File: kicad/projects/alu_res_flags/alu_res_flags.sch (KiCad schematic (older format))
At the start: 56 parts, among them J1 RES_CRRYBRRW_EQ_IN, J2 Aux_connection, J3 Bus_connection, J4 Control_signal_backplane, J5 ECNZ_OUT, U1 74HCT04, U10 74HCT245, U11 74HCT173, U12 74HCT245, U2 74HCT377, U3 74HCT377, U4 74HCT245, U5 74HCT245, U6 74HCT27, U7 74HCT27, U8 74HCT30, U9 74HCT245

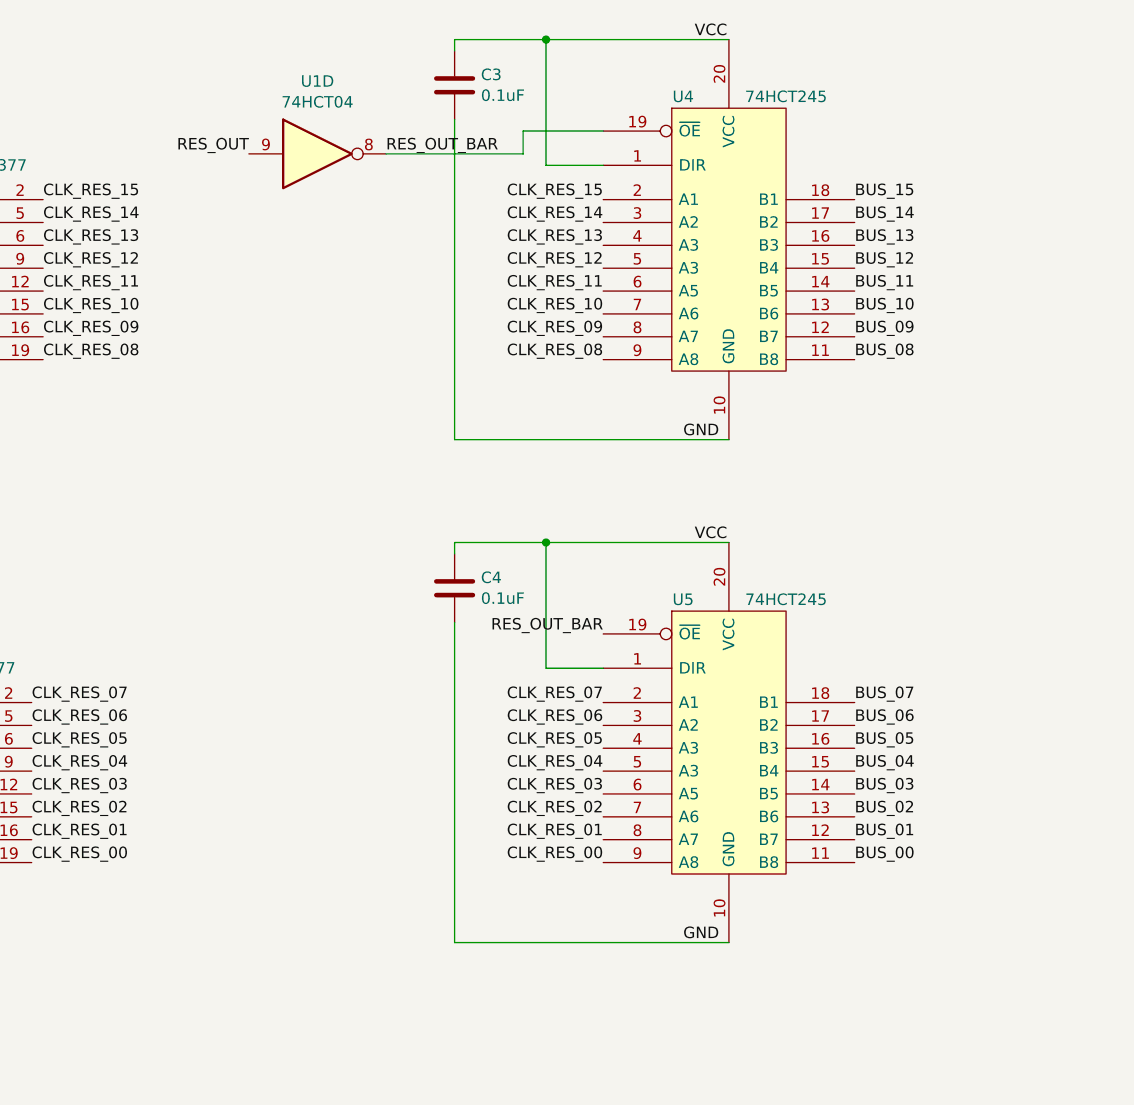
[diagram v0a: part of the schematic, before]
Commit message: Initial component placement
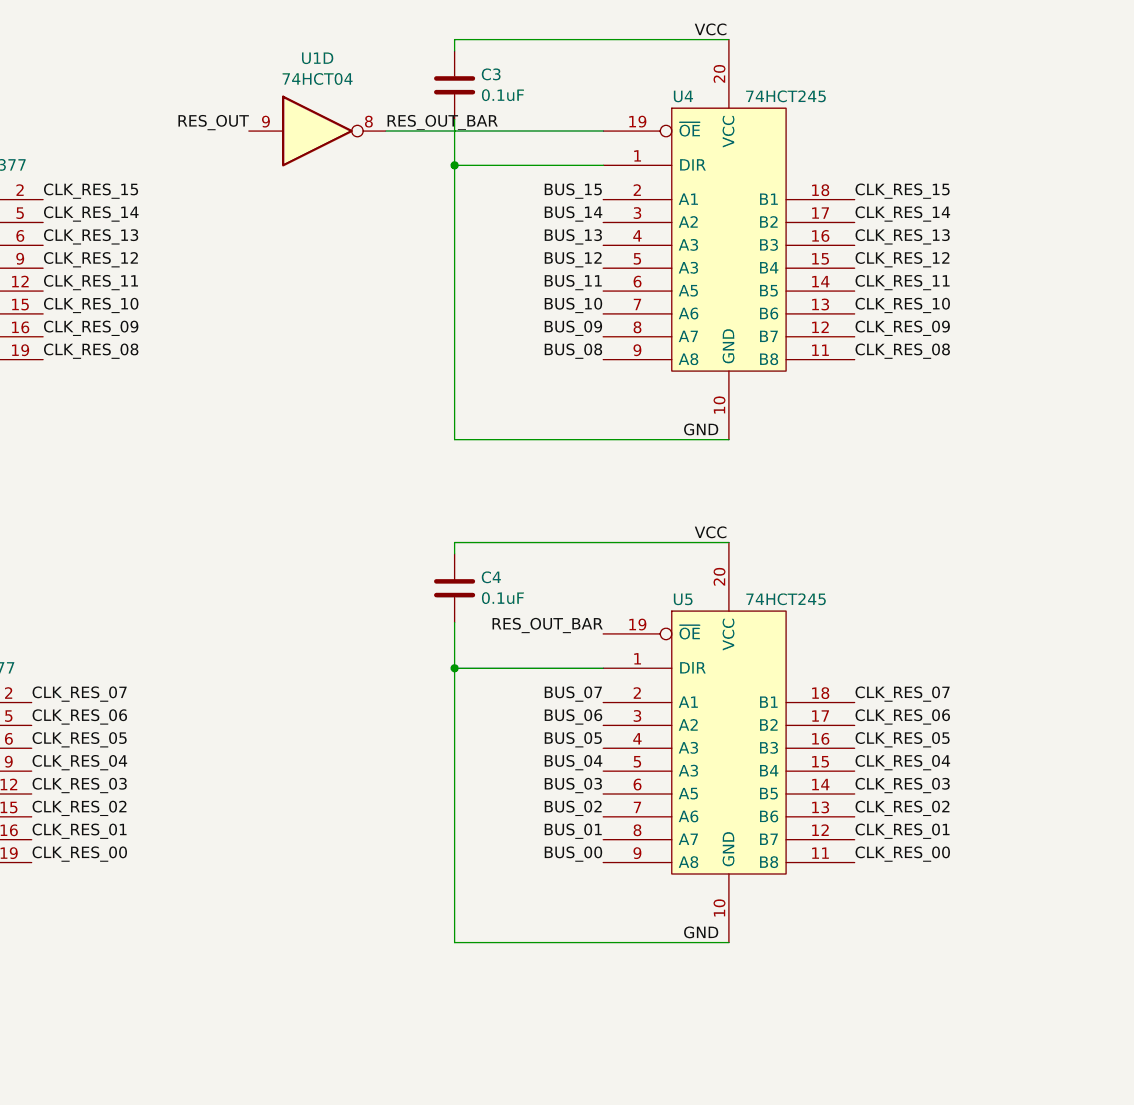
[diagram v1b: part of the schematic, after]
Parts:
- C1, C10, C11, C12, C2, C3, C4, C5, C6, C7, C8, C9: footprint (none) -> Capacitor_THT:C_Disc_D4.7mm_W2.5mm_P5.00mm
- D1, D10, D11, D12, D13, D14, D15, D16, D17, D18, D19, D2, D20, D21, D22, D23, D24, D3, D4, D5, D6, D7, D8, D9: footprint (none) -> eight-bit-computer:LED_D5.0mm_Horizontal_O3.81mm_Z3.0mm
- J1: footprint (none) -> Connector_PinSocket_2.54mm:PinSocket_1x19_P2.54mm_Horizontal
- J2: footprint (none) -> Connector_PinHeader_2.54mm:PinHeader_1x10_P2.54mm_Horizontal
- J3: footprint (none) -> Connector_PinHeader_2.54mm:PinHeader_1x16_P2.54mm_Horizontal
- J4: footprint (none) -> eight-bit-computer:backplane-connector
- J5: footprint (none) -> Connector_PinSocket_2.54mm:PinSocket_1x04_P2.54mm_Horizontal
- U1, U6, U7, U8: footprint (none) -> Package_DIP:DIP-14_W7.62mm_Socket
- U10, U12, U2, U3, U4, U5, U9: footprint (none) -> Package_DIP:DIP-20_W7.62mm_Socket
- U11: footprint (none) -> Package_DIP:DIP-16_W7.62mm_Socket
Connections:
- net BUS_00: now also U5.9 (A8); no longer U5.11 (B8)
- net BUS_01: now also U5.8 (A7); no longer U5.12 (B7)
- net BUS_02: now also U5.7 (A6); no longer U5.13 (B6)
- net BUS_03: now also U5.6 (A5); no longer U5.14 (B5)
- net BUS_04: now also U5.5 (A3); no longer U5.15 (B4)
- net BUS_05: now also U5.4 (A3); no longer U5.16 (B3)
- net BUS_06: now also U5.3 (A2); no longer U5.17 (B2)
- net BUS_07: now also U5.2 (A1); no longer U5.18 (B1)
- net BUS_08: now also U4.9 (A8); no longer U4.11 (B8)
- net BUS_09: now also U4.8 (A7); no longer U4.12 (B7)
- net BUS_10: now also U4.7 (A6); no longer U4.13 (B6)
- net BUS_11: now also U4.6 (A5); no longer U4.14 (B5)
- net BUS_12: now also U4.5 (A3); no longer U4.15 (B4)
- net BUS_13: now also U4.4 (A3); no longer U4.16 (B3)
- net BUS_14: now also U4.3 (A2); no longer U4.17 (B2)
- net BUS_15: now also U4.2 (A1); no longer U4.18 (B1)
- net CLK_RES_00: now also U5.11 (B8); no longer U5.9 (A8)
- net CLK_RES_01: now also U5.12 (B7); no longer U5.8 (A7)
- net CLK_RES_02: now also U5.13 (B6); no longer U5.7 (A6)
- net CLK_RES_03: now also U5.14 (B5); no longer U5.6 (A5)
- net CLK_RES_04: now also U5.15 (B4); no longer U5.5 (A3)
- net CLK_RES_05: now also U5.16 (B3); no longer U5.4 (A3)
- net CLK_RES_06: now also U5.17 (B2); no longer U5.3 (A2)
- net CLK_RES_07: now also U5.18 (B1); no longer U5.2 (A1)
- net CLK_RES_08: now also U4.11 (B8); no longer U4.9 (A8)
- net CLK_RES_09: now also U4.12 (B7); no longer U4.8 (A7)
- net CLK_RES_10: now also U4.13 (B6); no longer U4.7 (A6)
- net CLK_RES_11: now also U4.14 (B5); no longer U4.6 (A5)
- net CLK_RES_12: now also U4.15 (B4); no longer U4.5 (A3)
- net CLK_RES_13: now also U4.16 (B3); no longer U4.4 (A3)
- net CLK_RES_14: now also U4.17 (B2); no longer U4.3 (A2)
- net CLK_RES_15: now also U4.18 (B1); no longer U4.2 (A1)
- net GND: now also U4.1 (DIR), U5.1 (DIR)
- net VCC: no longer U4.1 (DIR), U5.1 (DIR)
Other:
- moved on the sheet: U1D

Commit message: Starting to route PCB.
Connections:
- net NEGATIVE renamed RES_15
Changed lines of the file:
@@
 Text Label 13300 8300 2    50   ~ 0
 CARRYBORROW
-Text Label 13300 8400 2    50   ~ 0
-NEGATIVE
 Text Label 13300 8500 2    50   ~ 0
 ZERO
@@
 Text Label 15950 7900 2    50   ~ 0
 CARRYBORROW
-Text Label 15950 8000 2    50   ~ 0
-NEGATIVE
 Text Label 15950 8100 2    50   ~ 0
 ZERO
@@
 	9550 4300 9550 4350
 Connection ~ 9550 4350
-Text Label 2700 9850 0    50   ~ 0
-NEGATIVE
-Wire Wire Line
-	2400 9850 2700 9850
 Wire Wire Line
 	5600 3900 6800 3900
@@
 Wire Wire Line
 	5300 2100 6250 2100
+Text Label 13300 8400 2    50   ~ 0
+RES_15
+Text Label 15950 8000 2    50   ~ 0
+RES_15
 $EndSCHEMATC

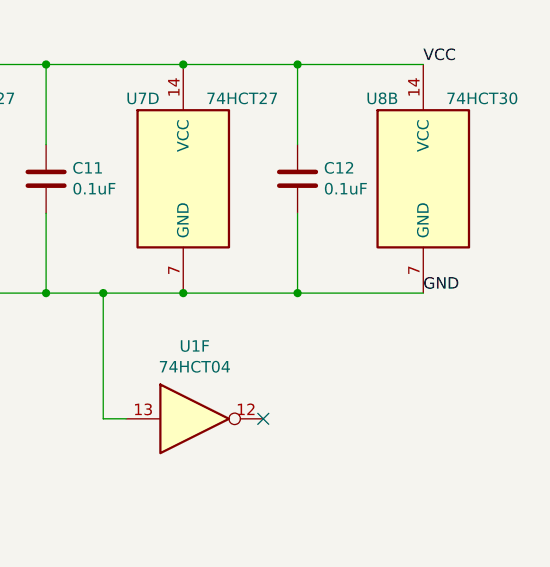
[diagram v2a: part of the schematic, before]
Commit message: Update HCT30 symbol and pins, more PCB routing.
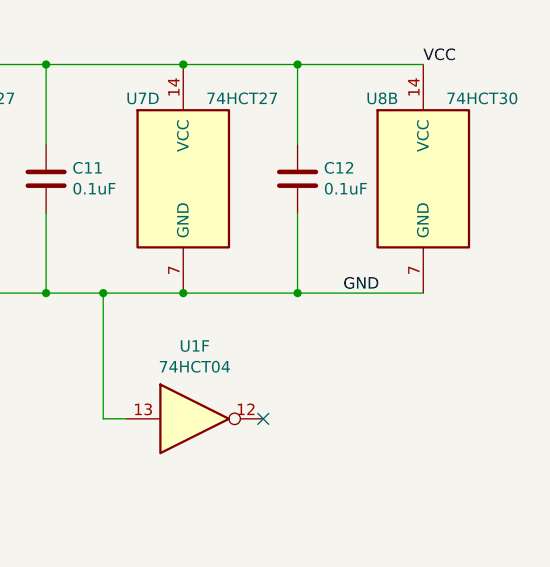
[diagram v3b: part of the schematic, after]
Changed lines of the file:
@@
 Text Label 19750 3250 0    50   ~ 0
 VCC
-Text Label 19750 4250 0    50   ~ 0
+Text Label 19400 4250 0    50   ~ 0
 GND
 NoConn ~ 19050 4800

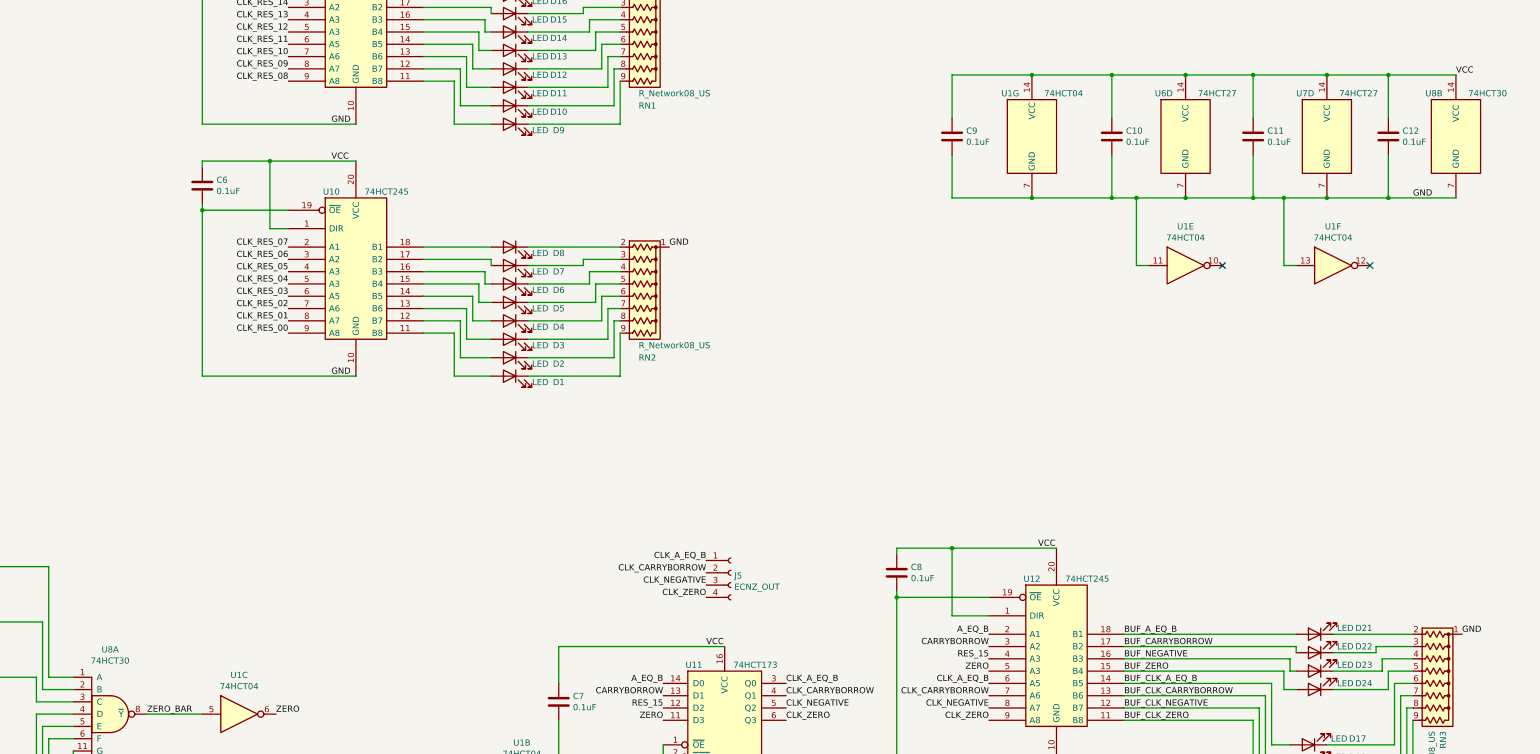
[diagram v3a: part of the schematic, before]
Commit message: Added almost all but LEDs to PCB
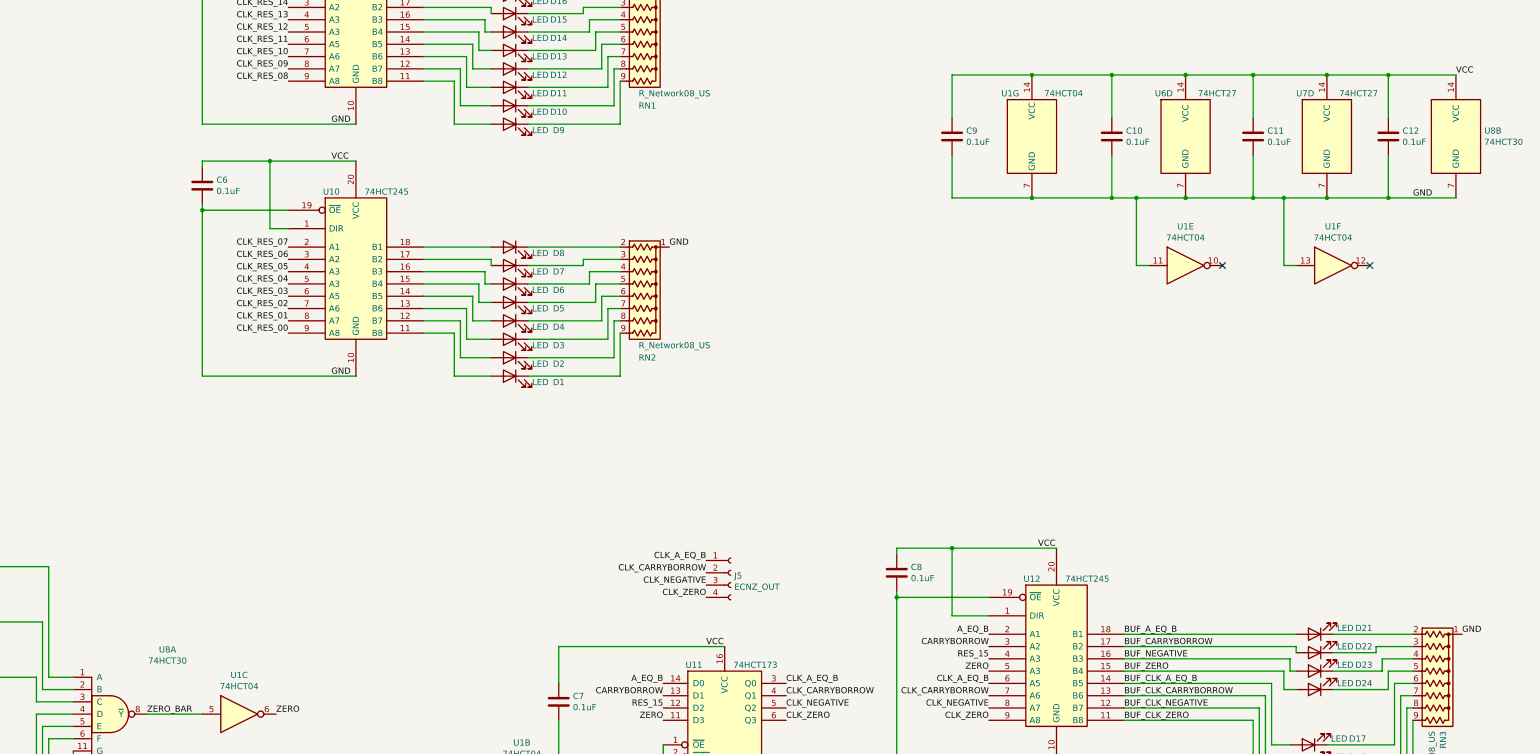
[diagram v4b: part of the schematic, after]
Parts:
- J1: footprint Connector_PinSocket_2.54mm:PinSocket_1x19_P2.54mm_Horizontal -> Connector_PinSocket_2.54mm:PinSocket_1x18_P2.54mm_Horizontal
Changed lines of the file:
@@
-$EndComp
-$Comp
-L eight-bit-computer:74HCT30 U8
-U 1 1 5FB1A22C
-P 8800 8450
-F 0 "U8" H 8800 8975 50  0000 C CNN
-F 1 "74HCT30" H 8800 8884 50  0000 C CNN
-F 2 "Package_DIP:DIP-14_W7.62mm_Socket" H 8800 8450 50  0001 C CNN
-F 3 "https://www.ti.com/lit/ds/symlink/cd74hct30.pdf" H 8800 8450 50  0001 C CNN
-	1    8800 8450
-	1    0    0    -1
-$EndComp
-$Comp
-L eight-bit-computer:74HCT30 U8
-U 2 1 5FB1BA54
-P 19750 3750
-F 0 "U8" H 19500 4100 50  0000 L CNN
-F 1 "74HCT30" H 19850 4100 50  0000 L CNN
-F 2 "Package_DIP:DIP-14_W7.62mm_Socket" H 19750 3750 50  0001 C CNN
-F 3 "https://www.ti.com/lit/ds/symlink/cd74hct30.pdf" H 19750 3750 50  0001 C CNN
-	2    19750 3750
-	1    0    0    -1
 $EndComp
 $Comp
@@
 F 0 "J1" H 2228 9126 50  0000 L CNN
 F 1 "RES_CRRYBRRW_EQ_IN" H 2228 9035 50  0000 L CNN
-F 2 "Connector_PinSocket_2.54mm:PinSocket_1x19_P2.54mm_Horizontal" H 2200 9150 50  0001 C CNN
+F 2 "Connector_PinSocket_2.54mm:PinSocket_1x18_P2.54mm_Horizontal" H 2200 9150 50  0001 C CNN
 F 3 "~" H 2200 9150 50  0001 C CNN
 	1    2200 9150
@@
 Text Label 15950 8000 2    50   ~ 0
 RES_15
+$Comp
+L eight-bit-computer:74HCT30 U8
+U 1 1 5FBBC8A7
+P 8800 8450
+F 0 "U8" H 9267 8975 50  0000 C CNN
+F 1 "74HCT30" H 9267 8884 50  0000 C CNN
+F 2 "Package_DIP:DIP-14_W7.62mm_Socket" H 8800 8450 50  0001 C CNN
+F 3 "https://www.ti.com/lit/ds/symlink/cd74hct30.pdf" H 8800 8450 50  0001 C CNN
+	1    8800 8450
+	1    0    0    -1
+$EndComp
+$Comp
+L eight-bit-computer:74HCT30 U8
+U 2 1 5FBBF1CA
+P 19750 3750
+F 0 "U8" H 19980 3796 50  0000 L CNN
+F 1 "74HCT30" H 19980 3705 50  0000 L CNN
+F 2 "Package_DIP:DIP-14_W7.62mm_Socket" H 19750 3750 50  0001 C CNN
+F 3 "https://www.ti.com/lit/ds/symlink/cd74hct30.pdf" H 19750 3750 50  0001 C CNN
+	2    19750 3750
+	1    0    0    -1
+$EndComp
 $EndSCHEMATC

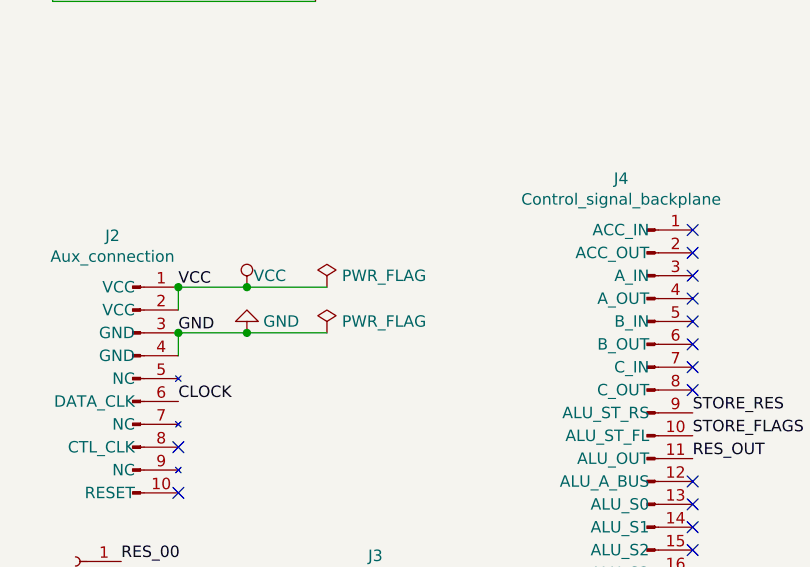
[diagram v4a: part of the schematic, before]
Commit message: Alu res and flags prepped for fab. Adjusted spacing between internonnect on ALU boards
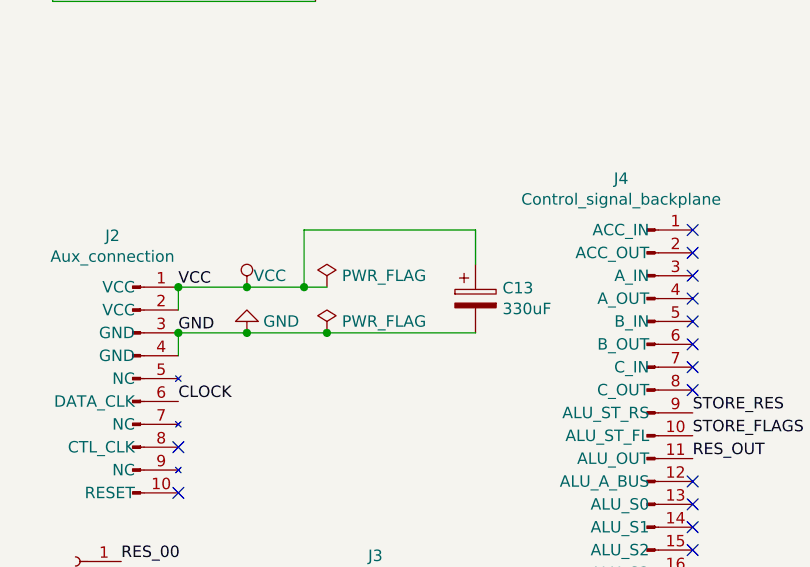
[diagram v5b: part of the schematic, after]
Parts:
- added C13: 330uF, Capacitor_THT:CP_Radial_D6.3mm_P2.50mm, symbol Device:CP
- J2: footprint Connector_PinHeader_2.54mm:PinHeader_1x10_P2.54mm_Horizontal -> eight-bit-computer:aux-connection
- J3: footprint Connector_PinHeader_2.54mm:PinHeader_1x16_P2.54mm_Horizontal -> eight-bit-computer:bus-connection
- J4: footprint eight-bit-computer:backplane-connector -> eight-bit-computer:backplane-connector-single-row-annotated
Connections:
- net GND: now also C13.2
- net VCC: now also C13.1
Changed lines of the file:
@@
 F 0 "J3" H 3512 10175 50  0000 C CNN
 F 1 "Bus_connection" H 3512 10084 50  0000 C CNN
-F 2 "Connector_PinHeader_2.54mm:PinHeader_1x16_P2.54mm_Horizontal" H 3550 9650 50  0001 C CNN
+F 2 "eight-bit-computer:bus-connection" H 3550 9650 50  0001 C CNN
 F 3 "~" H 3550 9650 50  0001 C CNN
 	1    3650 9250
@@
 F 0 "J4" H 4587 10125 50  0000 C CNN
 F 1 "Control_signal_backplane" H 4587 10034 50  0000 C CNN
-F 2 "eight-bit-computer:backplane-connector" H 4700 8400 50  0001 C CNN
+F 2 "eight-bit-computer:backplane-connector-single-row-annotated" H 4700 8400 50  0001 C CNN
 F 3 "~" H 4700 8400 50  0001 C CNN
 	1    4700 8400
@@
 F 0 "J2" H 2362 8175 50  0000 C CNN
 F 1 "Aux_connection" H 2362 8084 50  0000 C CNN
-F 2 "Connector_PinHeader_2.54mm:PinHeader_1x10_P2.54mm_Horizontal" H 2450 7550 50  0001 C CNN
+F 2 "eight-bit-computer:aux-connection" H 2450 7550 50  0001 C CNN
 F 3 "~" H 2450 7550 50  0001 C CNN
 	1    2450 7550
@@
 Connection ~ 2950 7150
 Wire Wire Line
-	2950 7150 3300 7150
+	2950 7150 3200 7150
 Wire Wire Line
 	2650 7350 2950 7350
@@
 	1    0    0    -1
 $EndComp
+$Comp
+L Device:CP C13
+U 1 1 5FCF3BAB
+P 3950 7200
+F 0 "C13" H 4068 7246 50  0000 L CNN
+F 1 "330uF" H 4068 7155 50  0000 L CNN
+F 2 "Capacitor_THT:CP_Radial_D6.3mm_P2.50mm" H 3988 7050 50  0001 C CNN
+F 3 "~" H 3950 7200 50  0001 C CNN
+	1    3950 7200
+	1    0    0    -1
+$EndComp
+Wire Wire Line
+	3300 7350 3950 7350
+Connection ~ 3300 7350
+Wire Wire Line
+	3950 7050 3950 6900
+Wire Wire Line
+	3950 6900 3200 6900
+Wire Wire Line
+	3200 6900 3200 7150
+Connection ~ 3200 7150
+Wire Wire Line
+	3200 7150 3300 7150
 $EndSCHEMATC
